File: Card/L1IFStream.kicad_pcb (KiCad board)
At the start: 4 copper layers, 146.9 x 117.4 mm, 112 parts, among them J1 Conn_Coaxial, J2 USB_A, J3 RF_Shield_One_Piece, J4 Conn_Coaxial, U1 MAX2769ETI+T, U10 74LVC374, U11 74HC2G04, U2 TPS717285DCKR, U3 TPS717285DCKR, U4 NCP164CSN330T1G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

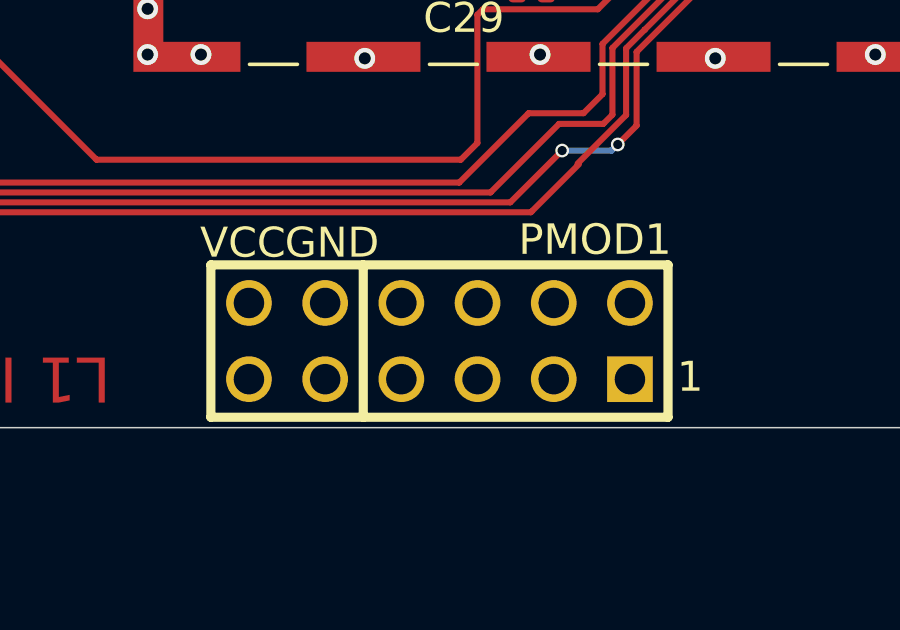
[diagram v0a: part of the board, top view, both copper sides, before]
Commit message: Added Tallysman Antenna Mount
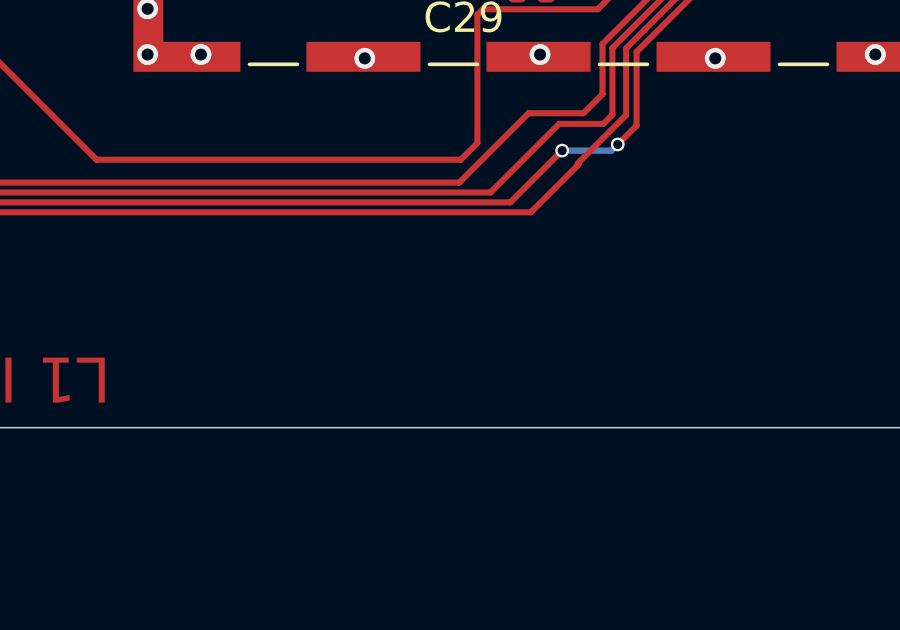
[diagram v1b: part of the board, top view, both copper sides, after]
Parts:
- removed PMOD1: PMOD-Device-x1-Type-1-GPIO, L1IFStream:pmod_pin_array_6x2
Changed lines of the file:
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@@
   (net 100 "unconnected-(U8-NC-Pad1)")
   (net 101 "Net-(D6-K)")
-  (net 102 "unconnected-(PMOD1-IO3-Pad4)")
-  (net 103 "unconnected-(PMOD1-VCC-Pad6)")
-  (net 104 "unconnected-(PMOD1-VCC-Pad12)")
   (footprint "L1IFStream:C_0805_2012Metric" (layer "F.Cu")
     (at 121.59 89.662)
@@
       (net 99 "unconnected-(X1-NC-Pad10)") (pinfunction "NC") (pintype "no_connect"))
   )
-  (footprint "L1IFStream:pmod_pin_array_6x2" (layer "F.Cu")
-    (at 152.8572 120.6754 -90)
-    (descr "QMOD Pin Header 2 x 6 pins")
-    (tags "CONN")
-    (property "Sheetfile" "L1IFStream.kicad_sch")
-    (property "Sheetname" "")
-    (property "ki_description" "PMOD Device Type 1 (GPIO)")
-    (property "ki_keywords" "PMOD, Digilent, Device, Type 1, GPIO")
-    (attr through_hole)
-    (fp_text reference "PMOD1" (at -3.3782 -5.1816 -180) (layer "F.SilkS")
-        (effects (font (size 1.016 1.016) (thickness 0.254)))
-    )
-    (fp_text value "PMOD-Device-x1-Type-1-GPIO" (at -3.5 0) (layer "Dwgs.User") hide
-        (effects (font (size 1.016 1.016) (thickness 0.2032)))
-    )
-    (fp_text user "GND" (at 4.318 3.81 90) (layer "B.SilkS")
-        (effects (font (size 1 1) (thickness 0.15)) (justify mirror))
-    )
-    (fp_text user "VCC" (at 4.318 6.35 90) (layer "B.SilkS")
-        (effects (font (size 1 1) (thickness 0.15)) (justify mirror))
-    )
-    (fp_text user "1" (at 3.556 -6.35 90) (layer "B.SilkS")
-        (effects (font (size 1 1) (thickness 0.15)) (justify mirror))
-    )
-    (fp_text user "GND" (at -3.2766 3.5814 -180) (layer "F.SilkS")
-        (effects (font (size 1 1) (thickness 0.15)))
-    )
-    (fp_text user "1" (at 1.1938 -8.3566 -180) (layer "F.SilkS")
-        (effects (font (size 1 1) (thickness 0.15)))
-    )
-    (fp_text user "VCC" (at -3.2766 6.5532 -180) (layer "F.SilkS")
-        (effects (font (size 1 1) (thickness 0.15)))
-    )
-    (fp_text user "Board Edge" (at -5.25 9.5) (layer "Dwgs.User")
-        (effects (font (size 0.127 0.127) (thickness 0.03175)))
-    )
-    (fp_text user "0.45\"" (at -7.5 4.75) (layer "Dwgs.User")
-        (effects (font (size 0.5 0.5) (thickness 0.125)))
-    )
-    (fp_text user "0.20\"" (at -2.5 8.5 90) (layer "Dwgs.User")
-        (effects (font (size 0.5 0.5) (thickness 0.125)))
-    )
-    (fp_text user "0.4\"" (at -6.25 4.75) (layer "Dwgs.User")
-        (effects (font (size 0.5 0.5) (thickness 0.125)))
-    )
-    (fp_line (start -2.54 -7.62) (end -2.54 7.62)
-      (stroke (width 0.3048) (type solid)) (layer "B.SilkS"))
-    (fp_line (start -2.54 7.62) (end 2.54 7.62)
-      (stroke (width 0.3048) (type solid)) (layer "B.SilkS"))
-    (fp_line (start 2.54 -7.62) (end -2.54 -7.62)
-      (stroke (width 0.3048) (type solid)) (layer "B.SilkS"))
-    (fp_line (start 2.54 2.54) (end -2.54 2.54)
-      (stroke (width 0.3048) (type solid)) (layer "B.SilkS"))
-    (fp_line (start 2.54 7.62) (end 2.54 -7.62)
-      (stroke (width 0.3048) (type solid)) (layer "B.SilkS"))
-    (fp_line (start -2.54 -7.62) (end -2.54 7.62)
-      (stroke (width 0.3048) (type solid)) (layer "F.SilkS"))
-    (fp_line (start -2.54 7.62) (end 2.54 7.62)
-      (stroke (width 0.3048) (type solid)) (layer "F.SilkS"))
-    (fp_line (start 2.54 -7.62) (end -2.54 -7.62)
-      (stroke (width 0.3048) (type solid)) (layer "F.SilkS"))
-    (fp_line (start 2.54 2.54) (end -2.54 2.54)
-      (stroke (width 0.3048) (type solid)) (layer "F.SilkS"))
-    (fp_line (start 2.54 7.62) (end 2.54 -7.62)
-      (stroke (width 0.3048) (type solid)) (layer "F.SilkS"))
-    (fp_line (start -6.985 0) (end -7.366 0.381)
-      (stroke (width 0.05) (type solid)) (layer "Dwgs.User"))
-    (fp_line (start -6.985 0) (end -6.985 11.43)
-      (stroke (width 0.05) (type solid)) (layer "Dwgs.User"))
-    (fp_line (start -6.985 11.43) (end -7.366 11.049)
-      (stroke (width 0.05) (type solid)) (layer "Dwgs.User"))
-    (fp_line (start -6.985 11.43) (end -6.604 11.049)
-      (stroke (width 0.05) (type solid)) (layer "Dwgs.User"))
-    (fp_line (start -6.604 0.381) (end -6.985 0)
-      (stroke (width 0.05) (type solid)) (layer "Dwgs.User"))
-    (fp_line (start -5.842 0) (end -6.223 0.381)
-      (stroke (width 0.05) (type solid)) (layer "Dwgs.User"))
-    (fp_line (start -5.842 0) (end -5.842 10.16)
-      (stroke (width 0.05) (type solid)) (layer "Dwgs.User"))
-    (fp_line (start -5.842 0) (end -5.461 0.381)
-      (stroke (width 0.05) (type solid)) (layer "Dwgs.User"))
-    (fp_line (start -5.842 10.16) (end -6.223 9.779)
-      (stroke (width 0.05) (type solid)) (layer "Dwgs.User"))
-    (fp_line (start -5.842 10.16) (end -5.461 9.779)
-      (stroke (width 0.05) (type solid)) (layer "Dwgs.User"))
-    (fp_line (start -5.08 -11.43) (end -4.445 -11.43)
-      (stroke (width 0.05) (type solid)) (layer "Dwgs.User"))
-    (fp_line (start -5.08 8.89) (end -4.826 8.636)
-      (stroke (width 0.05) (type solid)) (layer "Dwgs.User"))
-    (fp_line (start -5.08 8.89) (end -4.826 9.144)
-      (stroke (width 0.05) (type solid)) (layer "Dwgs.User"))
-    (fp_line (start -5.08 10.16) (end -5.08 -10.16)
-      (stroke (width 0.05) (type solid)) (layer "Dwgs.User"))
-    (fp_line (start -5.08 11.43) (end -4.445 11.43)
-      (stroke (width 0.05) (type solid)) (layer "Dwgs.User"))
-    (fp_line (start -3.81 -11.43) (end -3.175 -11.43)
-      (stroke (width 0.05) (type solid)) (layer "Dwgs.User"))
-    (fp_line (start -3.81 11.43) (end -3.175 11.43)
-      (stroke (width 0.05) (type solid)) (layer "Dwgs.User"))
-    (fp_line (start -2.54 -11.43) (end -1.905 -11.43)
-      (stroke (width 0.05) (type solid)) (layer "Dwgs.User"))
-    (fp_line (start -2.54 11.43) (end -1.905 11.43)
-      (stroke (width 0.05) (type solid)) (layer "Dwgs.User"))
-    (fp_line (start -1.27 -11.43) (end -0.635 -11.43)
-      (stroke (width 0.05) (type solid)) (layer "Dwgs.User"))
-    (fp_line (start -1.27 11.43) (end -0.635 11.43)
-      (stroke (width 0.05) (type solid)) (layer "Dwgs.User"))
-    (fp_line (start -0.254 8.636) (end 0 8.89)
-      (stroke (width 0.05) (type solid)) (layer "Dwgs.User"))
-    (fp_line (start 0 -11.43) (end 0.635 -11.43)
-      (stroke (width 0.05) (type solid)) (layer "Dwgs.User"))
-    (fp_line (start 0 -10.16) (end -5.08 -10.16)
-      (stroke (width 0.05) (type solid)) (layer "Dwgs.User"))
-    (fp_line (start 0 8.89) (end -5.08 8.89)
-      (stroke (width 0.05) (type solid)) (layer "Dwgs.User"))
-    (fp_line (start 0 8.89) (end -0.254 9.144)
-      (stroke (width 0.05) (type solid)) (layer "Dwgs.User"))
-    (fp_line (start 0 10.16) (end -5.08 10.16)
-      (stroke (width 0.05) (type solid)) (layer "Dwgs.User"))
-    (fp_line (start 0 11.43) (end 0.635 11.43)
-      (stroke (width 0.05) (type solid)) (layer "Dwgs.User"))
-    (fp_line (start 1.27 -11.43) (end 1.905 -11.43)
-      (stroke (width 0.05) (type solid)) (layer "Dwgs.User"))
-    (fp_line (start 1.27 11.43) (end 1.905 11.43)
-      (stroke (width 0.05) (type solid)) (layer "Dwgs.User"))
-    (fp_line (start 2.54 -11.43) (end 3.175 -11.43)
-      (stroke (width 0.05) (type solid)) (layer "Dwgs.User"))
-    (pad "1" thru_hole rect (at 1.27 -6.35 270) (size 1.524 1.524) (drill 1.016) (layers "*.Cu" "*.Mask" "F.SilkS")
-      (net 18 "/I0") (pinfunction "IO0") (pintype "bidirectional"))
-    (pad "2" thru_hole circle (at 1.27 -3.81 180) (size 1.524 1.524) (drill 1.016) (layers "*.Cu" "*.Mask" "F.SilkS")
-      (net 19 "/I1") (pinfunction "IO1") (pintype "bidirectional"))
-    (pad "3" thru_hole circle (at 1.27 -1.27 180) (size 1.524 1.524) (drill 1.016) (layers "*.Cu" "*.Mask" "F.SilkS")
-      (net 27 "/CLKOUT") (pinfunction "IO2") (pintype "bidirectional"))
-    (pad "4" thru_hole circle (at 1.27 1.27 180) (size 1.524 1.524) (drill 1.016) (layers "*.Cu" "*.Mask" "F.SilkS")
-      (net 102 "unconnected-(PMOD1-IO3-Pad4)") (pinfunction "IO3") (pintype "bidirectional+no_connect"))
-    (pad "5" thru_hole circle (at 1.27 3.81 180) (size 1.524 1.524) (drill 1.016) (layers "*.Cu" "*.Mask" "F.SilkS")
-      (net 4 "GND") (pinfunction "GND") (pintype "power_out"))
-    (pad "6" thru_hole circle (at 1.27 6.35 180) (size 1.524 1.524) (drill 1.016) (layers "*.Cu" "*.Mask" "F.SilkS")
-      (net 103 "unconnected-(PMOD1-VCC-Pad6)") (pinfunction "VCC") (pintype "power_out+no_connect"))
-    (pad "7" thru_hole circle (at -1.27 -6.35 180) (size 1.524 1.524) (drill 1.016) (layers "*.Cu" "*.Mask" "F.SilkS")
-      (net 17 "/Q0") (pinfunction "IO0") (pintype "bidirectional"))
-    (pad "8" thru_hole circle (at -1.27 -3.81 180) (size 1.524 1.524) (drill 1.016) (layers "*.Cu" "*.Mask" "F.SilkS")
-      (net 16 "/Q1") (pinfunction "IO1") (pintype "bidirectional"))
-    (pad "9" thru_hole circle (at -1.27 -1.27 180) (size 1.524 1.524) (drill 1.016) (layers "*.Cu" "*.Mask" "F.SilkS")
-      (net 75 "/~{TXE}") (pinfunction "IO2") (pintype "bidirectional"))
-    (pad "10" thru_hole circle (at -1.27 1.27 180) (size 1.524 1.524) (drill 1.016) (layers "*.Cu" "*.Mask" "F.SilkS")
-      (net 76 "/CLKIN") (pinfunction "IO3") (pintype "bidirectional"))
-    (pad "11" thru_hole circle (at -1.27 3.81 180) (size 1.524 1.524) (drill 1.016) (layers "*.Cu" "*.Mask" "F.SilkS")
-      (net 4 "GND") (pinfunction "GND") (pintype "power_out"))
-    (pad "12" thru_hole circle (at -1.27 6.35 180) (size 1.524 1.524) (drill 1.016) (layers "*.Cu" "*.Mask" "F.SilkS")
-      (net 104 "unconnected-(PMOD1-VCC-Pad12)") (pinfunction "VCC") (pintype "power_out+no_connect"))
-    (model "/usr/share/kicad/modules/packages3d/Socket_Strips.3dshapes/Socket_Strip_Angled_2x06.wrl"
-      (offset (xyz 0 5.079999924 0))
-      (scale (xyz 1 1 1))
-      (rotate (xyz 0 0 180))
-    )
-  )
   (footprint "L1IFStream:C_0402_1005Metric" (layer "F.Cu")

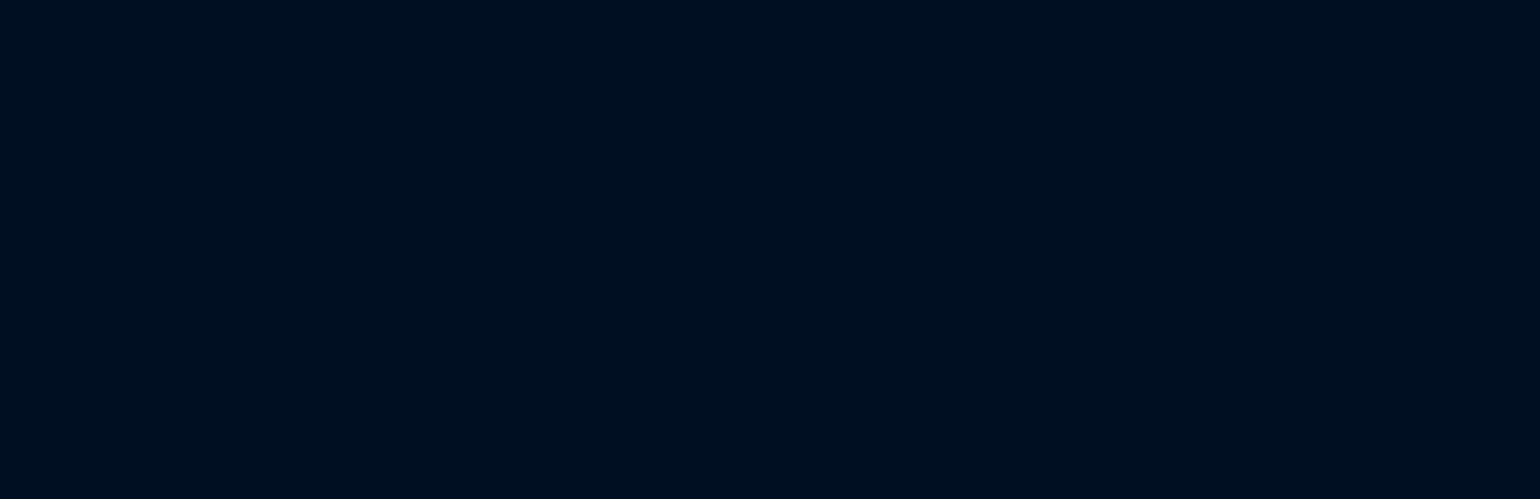
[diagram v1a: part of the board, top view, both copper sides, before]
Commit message: Added Thumb Drive Outline
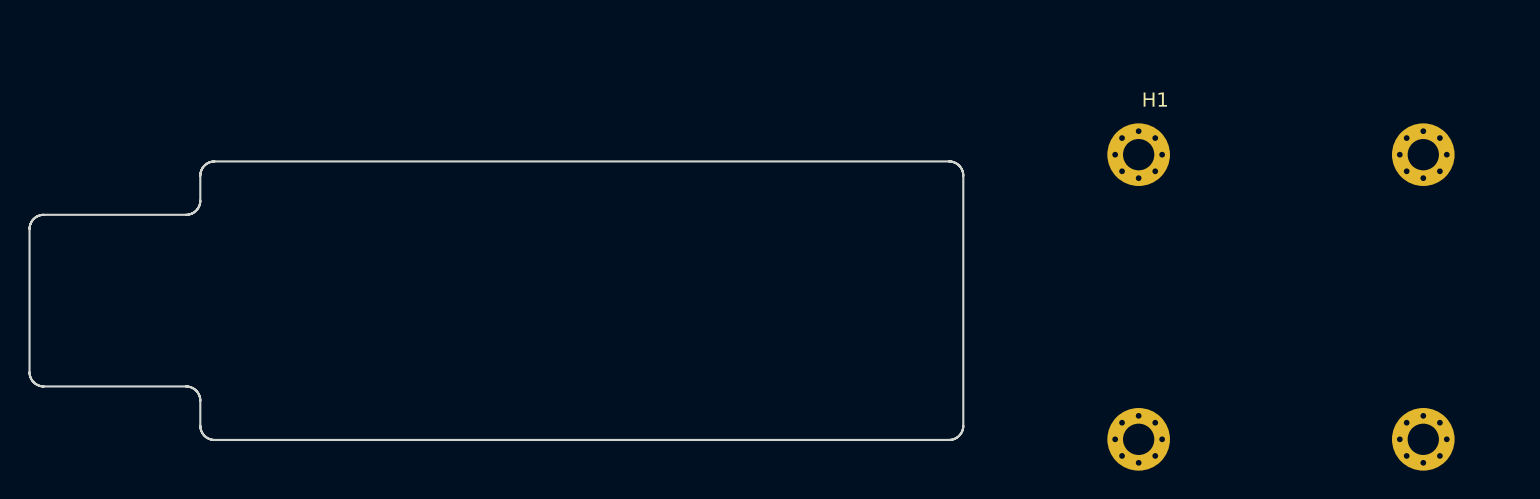
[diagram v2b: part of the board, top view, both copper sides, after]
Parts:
- added H1: MountingHole_Pad, L1IFStream:Mounts_2.2mm_M2_Pad_Via, F.Cu at (101.5, 173.6)
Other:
- board size 146.9 x 117.4 mm -> 156.3 x 119.7 mm

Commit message: Potential Board Layout
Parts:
- added J4: Conn_Coaxial, L1IFStream:MMCX_Molex_73415-1471_Vertical, F.Cu at (87.7, 182.8)
- added REF**: Laird_Technologies_97-2003_12.70x13.37mm, RF_Shielding:Laird_Technologies_97-2003_12.70x13.37mm, F.Cu at (78.4, 182.5)
- added U1: MAX2769ETI+T, L1IFStream:MAX2769ETI&plus_T, F.Cu at (80.3, 182.4)
- added U2: TPS717285DCKR, L1IFStream:TPS717285DCKR, F.Cu at (73.8, 179.3)
- added U3: TPS717285DCKR, L1IFStream:TPS717285DCKR, F.Cu at (74.0, 182.9)
- added U4: NCP164CSN330T1G, L1IFStream:TSOT-23-5, F.Cu at (38.3, 188.8)
- added U5: 93LC66BT-I_OT, L1IFStream:93LC66BT-I&slash_OT, F.Cu at (40.4, 175.3)
- added U6: FT2232H-Interface_USB, L1IFStream:LQFP-64_10x10mm_P0.5mm, F.Cu at (50.1, 181.3)
- added U9: 74LVC374, L1IFStream:TSSOP-20_4.4x6.5mm_P0.65mm, F.Cu at (63.1, 178.7)
- added U9: 74LVC374, L1IFStream:TSSOP-20_4.4x6.5mm_P0.65mm, F.Cu at (63.4, 186.1)
- added X1: SIT5156, L1IFStream:10L_CQFN, F.Cu at (75.4, 186.8)
- added X2: SIT2024BA-S8-33E-12.00000E, L1IFStream:SIT2024BA-S8-33E-12.000000E, F.Cu at (39.3, 180.4)
- added X3: QPQ1060, L1IFStream:Filter_SAW-5_1.4x1.2mm, F.Cu at (79.7, 178.0)
- moved H1 36.9 mm to (64.6, 173.6)
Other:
- board size 156.3 x 119.7 mm -> 156.3 x 127.3 mm
